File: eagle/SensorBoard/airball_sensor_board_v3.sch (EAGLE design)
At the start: 28 parts

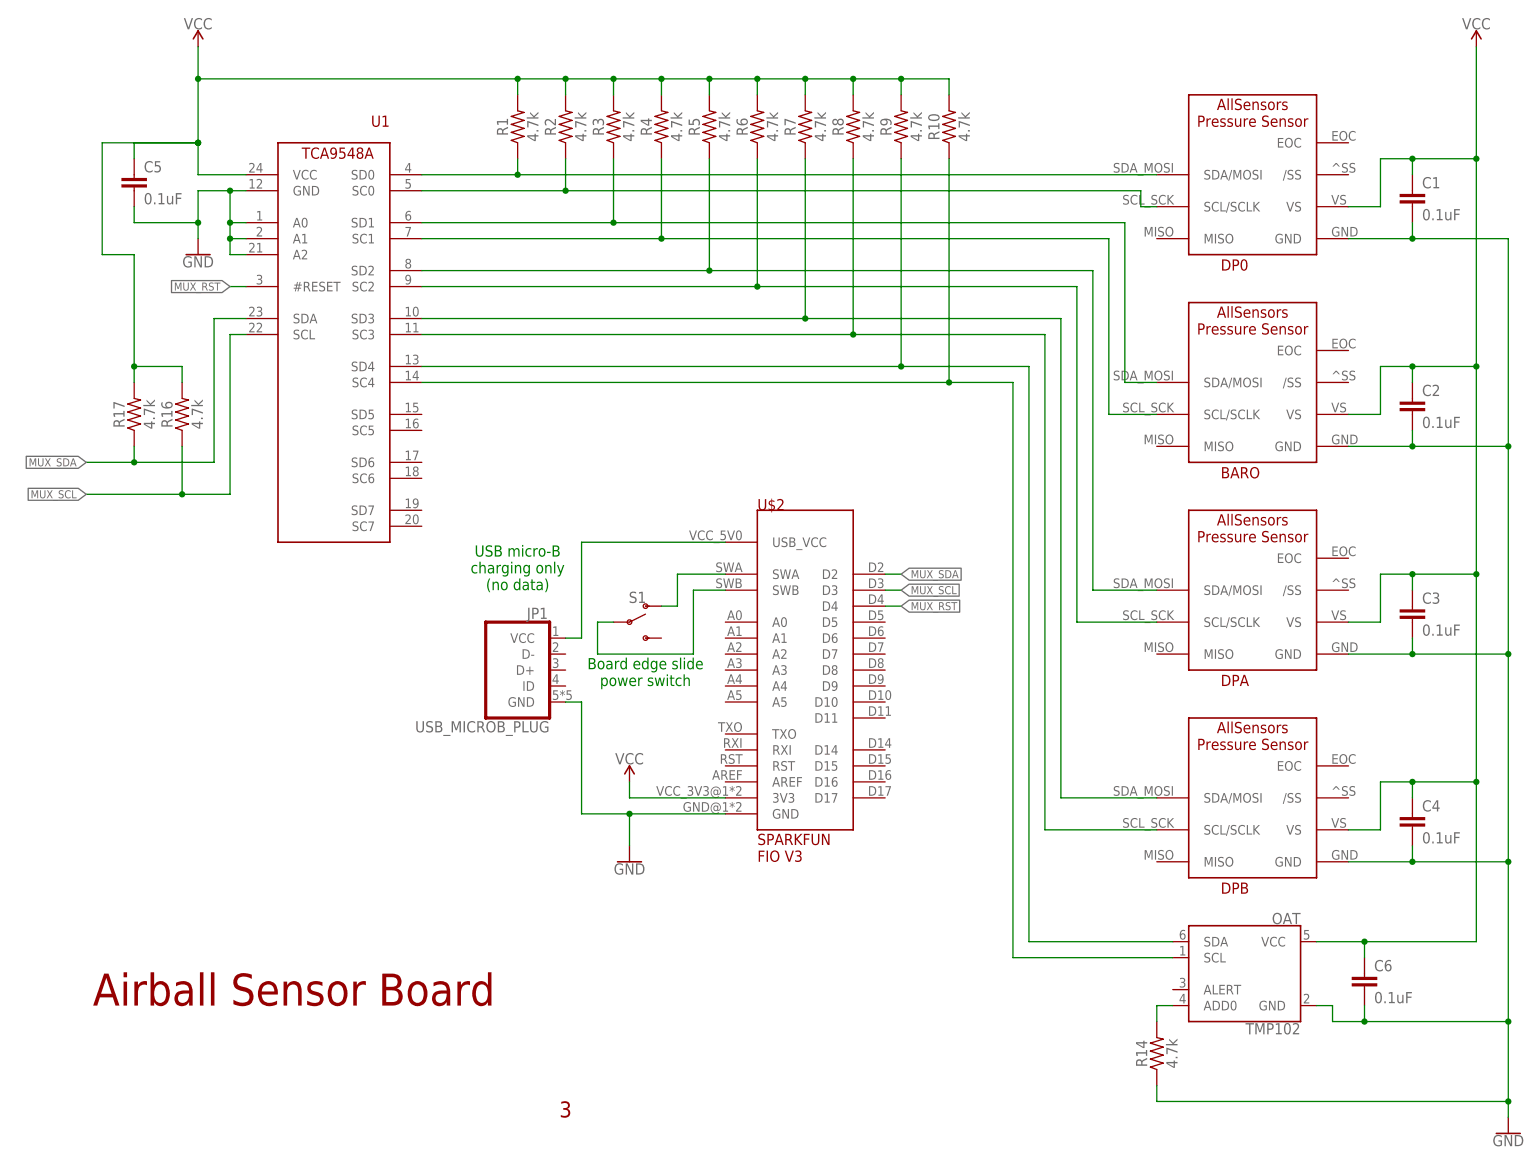
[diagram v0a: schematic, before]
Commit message: Cleanup of EAGLE libraries
Several parts were added to the unrelated library microbuilder.lbr;
migrate those to a new airball.lbr library file, and delete
microbuilder. Adjust airball_sensor_board_v3 to reference the new
library and adjust schematic device placement for minor cleanups.
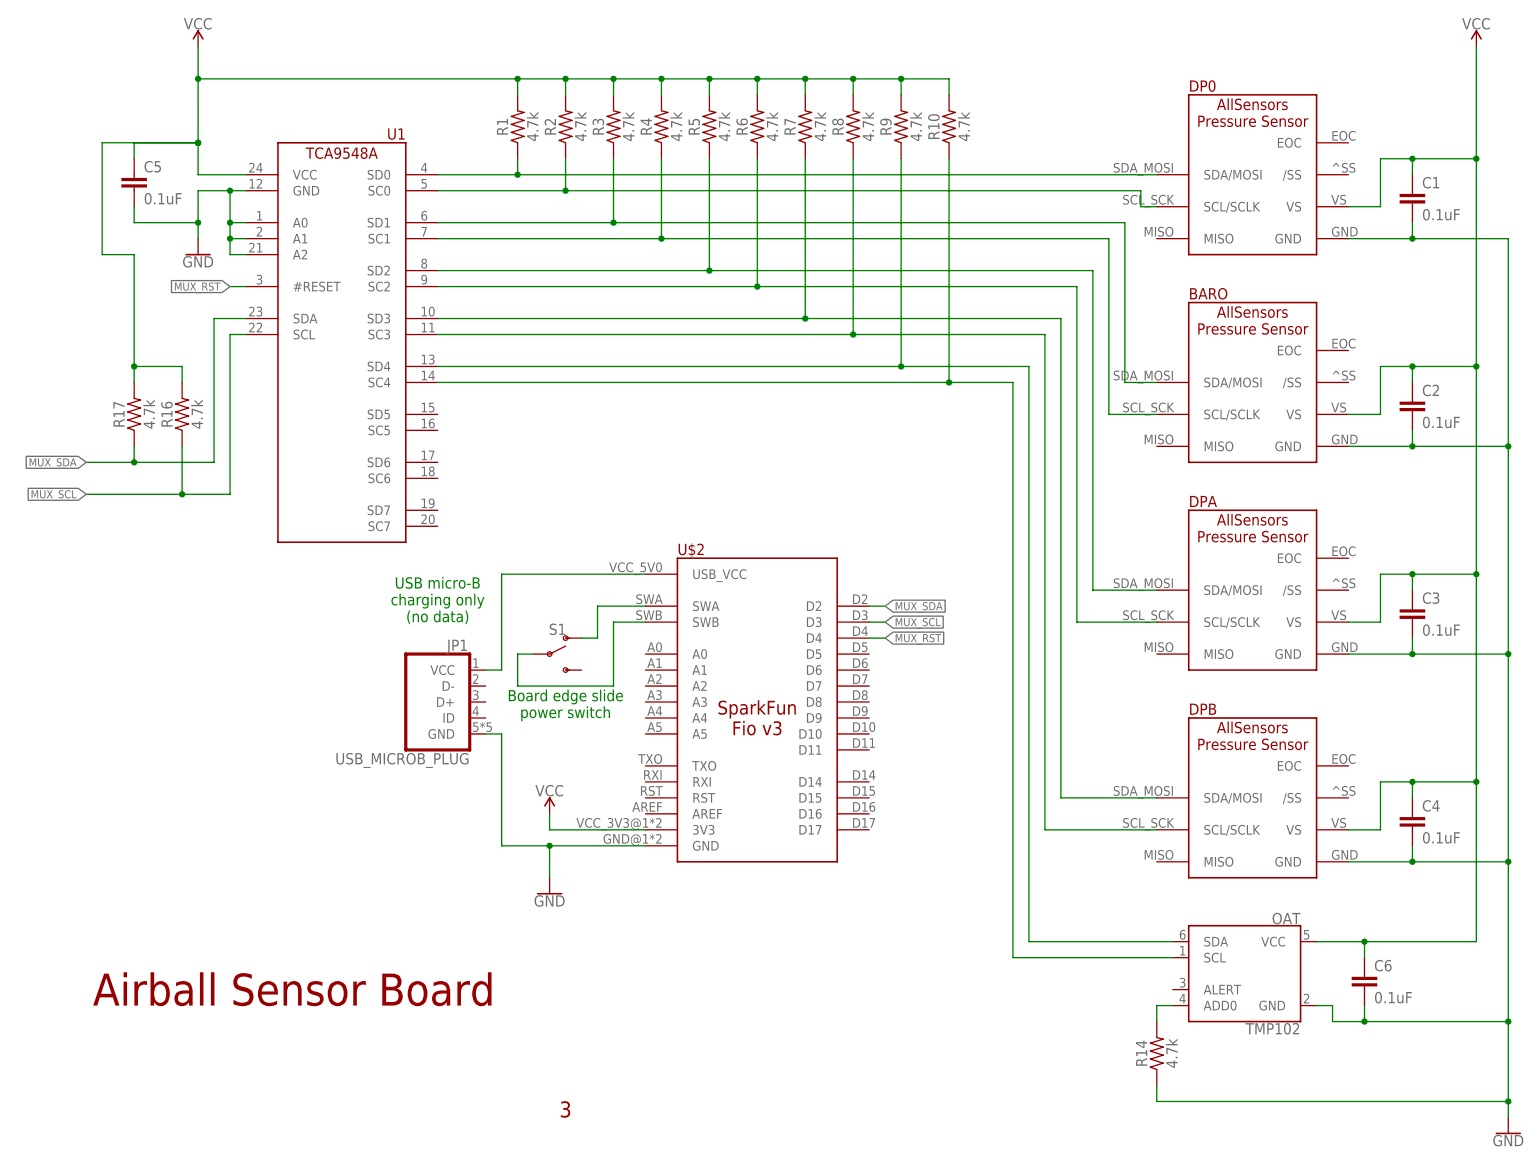
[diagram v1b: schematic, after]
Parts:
- BARO, DP0, DPA, DPB: device microbuilder:ALL_SENSORS_DLHR_E1ND -> airball:ALL_SENSORS_DLHR_E1ND
- JP1: device jcole:USB_MICROB_PLUG -> airball:USB_MICROB_PLUG
- U$2: device microbuilder:SPARKFUN_FIO_V3 -> airball:SPARKFUN_FIO_V3
- U1: device microbuilder:TCA9548ATSSOP24 -> airball:TCA9548ATSSOP24
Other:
- moved on the sheet: JP1, S1, U$2, U1
